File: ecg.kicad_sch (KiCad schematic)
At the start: 28 parts, among them SW1 SW_Push, SW2 SW_Push, U1 ESP32-S3-PICO-1-N8R2, U2 AD620, U3 OPA358

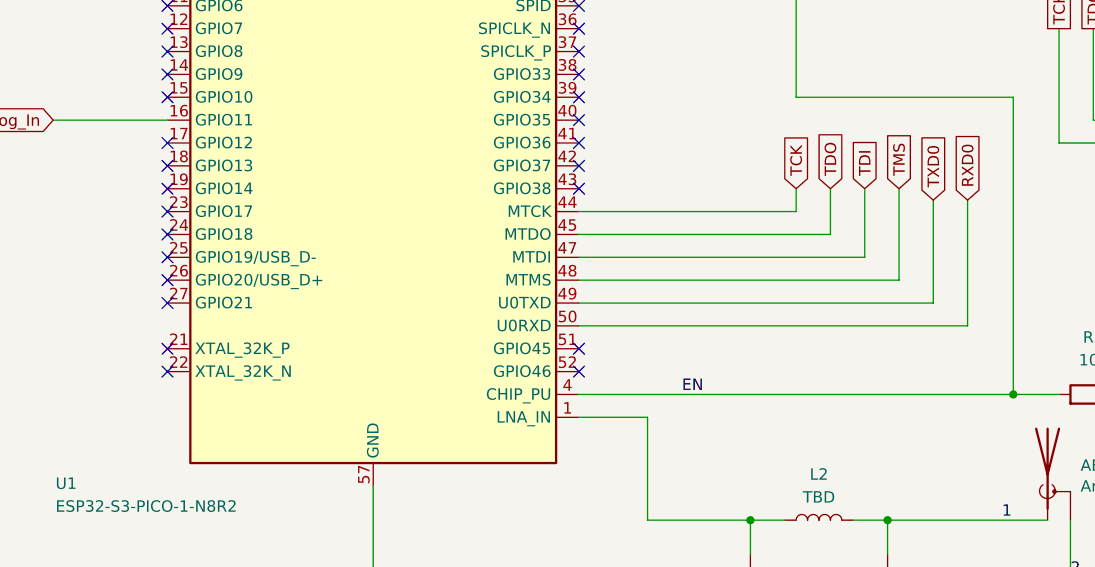
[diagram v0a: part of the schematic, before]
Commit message: Add 499ohm resistor for UART
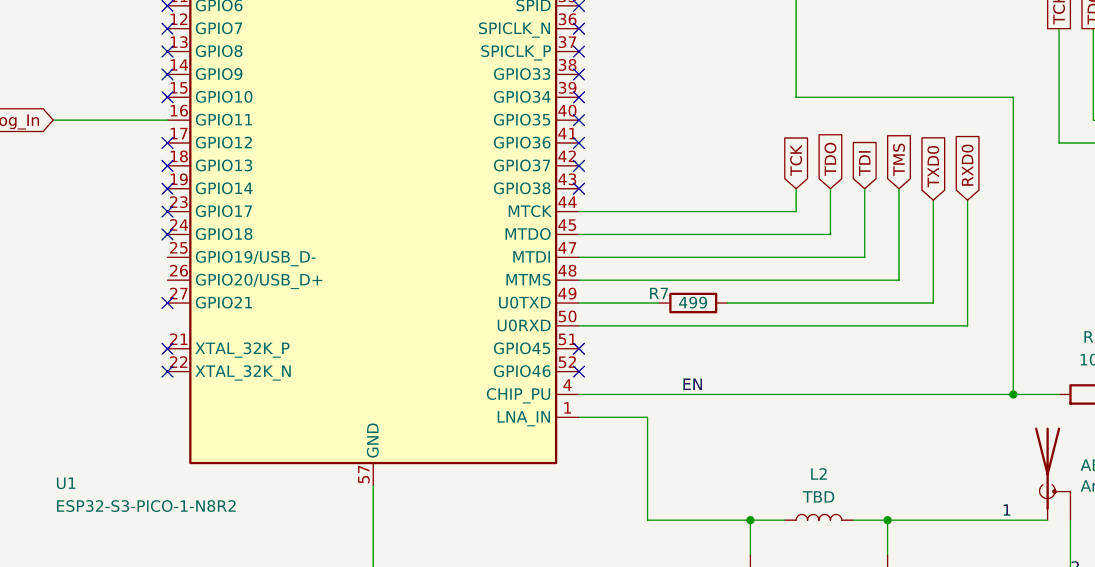
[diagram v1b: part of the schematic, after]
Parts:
- added R7: 499, symbol Device:R
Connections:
- net TDO: now also R7.2; no longer U1.49 (U0TXD)
- new net: R7.1, U1.49 (U0TXD)
- no-connect marks 38 -> 36
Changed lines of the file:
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@@
 	)
 	(no_connect
-		(at 86.36 154.94)
-	)
-	(no_connect
 		(at 86.36 139.7)
 	)
@@
 	)
 	(no_connect
-		(at 86.36 152.4)
-	)
-	(no_connect
 		(at 86.36 142.24)
 	)
@@
 	(wire
 		(pts
-			(xy 132.08 157.48) (xy 171.45 157.48)
-		)
-		(stroke
-			(width 0)
-			(type default)
-		)
-	)
-	(wire
-		(pts
 			(xy 368.3 134.62) (xy 368.3 162.56)
 		)
@@
 	(wire
 		(pts
+			(xy 148.59 157.48) (xy 171.45 157.48)
+		)
+		(stroke
+			(width 0)
+			(type default)
+		)
+	)
+	(wire
+		(pts
 			(xy 166.37 266.7) (xy 173.99 266.7)
 		)
@@
 	(wire
 		(pts
+			(xy 132.08 157.48) (xy 140.97 157.48)
+		)
+		(stroke
+			(width 0)
+			(type default)
+		)
+	)
+	(wire
+		(pts
 			(xy 166.37 196.85) (xy 151.13 196.85)
 		)
@@
 					(unit 1)
 				)
+			)
+		)
+	)
+	(symbol
+		(lib_id "Device:R")
+		(at 144.78 157.48 90)
+		(unit 1)
+		(exclude_from_sim no)
+		(in_bom yes)
+		(on_board yes)
+		(dnp no)
+		(property "Reference" "R7"
+			(at 140.97 156.464 90)
+			(effects
+				(font
+					(size 1.27 1.27)
+				)
+			)
+		)
+		(property "Value" "499"
+			(at 144.78 157.48 90)
+			(effects
+				(font
+					(size 1.27 1.27)
+				)
+			)
+		)
+		(property "Footprint" ""
+			(at 144.78 159.258 90)
+			(effects
+				(font
+					(size 1.27 1.27)
+				)
+				(hide yes)
+			)
+		)
+		(property "Datasheet" "~"
+			(at 144.78 157.48 0)
+			(effects
+				(font
+					(size 1.27 1.27)
+				)
+				(hide yes)
+			)
+		)
+		(property "Description" "Resistor"
+			(at 144.78 157.48 0)
+			(effects
+				(font
+					(size 1.27 1.27)
+				)
+				(hide yes)
+			)
+		)
+		(pin "2"
+		)
+		(pin "1"
+		)
+		(instances
+			(project "ecg"
+				(path "/78da8bdf-e40e-495b-ba6c-b18ee9000176"
+					(reference "R7")
+					(unit 1)
+				)

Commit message: A lot of changes!!!
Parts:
- removed AE2: Antenna_Shield, Connector_Coaxial:U.FL_Hirose_U.FL-R-SMT-1_Vertical, symbol Device:Antenna_Shield
- removed C7: 0.8 pF, Capacitor_SMD:C_0402_1005Metric, symbol Device:C
- removed L1: 3.9 nH, Inductor_SMD:L_0402_1005Metric, symbol Device:L
- added USB1: ~, symbol usb:USB_Blackbox
- AE1: footprint Connector_Coaxial:U.FL_Hirose_U.FL-R-SMT-1_Vertical -> RF_Antenna:Texas_SWRA117D_2.4GHz_Left
- C11, C12: value TBD -> 1.8 pF
- L2: value TBD -> 2.4 nH; footprint (none) -> Inductor_SMD:L_0201_0603Metric
- R7: footprint (none) -> Resistor_SMD:R_0201_0603Metric
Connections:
- net Analog_Out is gone; now on net Analog_In: C5.2, U3.1, U3.4 (-)
- net RXD0: no longer AE1.2 (Shield), BT1.2 (-), C1.1, C11.2, C12.2, C2.1, C3.1, C4.1, JTAG1. (4), SW1.1, SW2.1, U1.44 (MTCK), U1.47 (MTDI), U1.57 (GND), U2.4 (Vs-), U3.2 (V-)
- net TDO: no longer R7.2, UART1. (GND)
- net TMS: no longer AE1.1 (A), BT2.1 (+), C1.2, C11.1, C2.2, L2.2, R1.1, U1.2 (VDD3P3), U1.20 (VDD3P3_RTC), U1.3 (VDD3P3), U1.46 (VDD3P3_CPU), U1.55 (VDDA), U1.56 (VDDA), U2.7 (Vs+), U3.5 (ENABLE), U3.6 (V+), UART1. (GND)
- net USB_D-: now reaches U1.25 (GPIO19/USB_D-)
- net USB_D-: now also USB1. (2)
- net USB_D+: now reaches U1.26 (GPIO20/USB_D+)
- net USB_D+: now also USB1. (2)
- new net: BT2.1 (+), C1.2, C2.2, R1.1, U1.2 (VDD3P3), U1.20 (VDD3P3_RTC), U1.3 (VDD3P3), U1.46 (VDD3P3_CPU), U1.55 (VDDA), U1.56 (VDDA), U2.7 (Vs+), U3.5 (ENABLE), U3.6 (V+), UART1. (GND)
- new net 1: AE1.1 (A), C11.1, L2.2
- new net 2: AE1.2 (Shield), BT1.2 (-), C1.1, C11.2, C12.2, C2.1, C3.1, C4.1, SW1.1, SW2.1, U1.57 (GND), U2.4 (Vs-), U3.2 (V-), UART1. (GND)
- new net TCK: JTAG1. (4), U1.44 (MTCK)
- new net TDI: JTAG1. (4), U1.47 (MTDI)
- new net TXD0: R7.2, UART1. (GND)

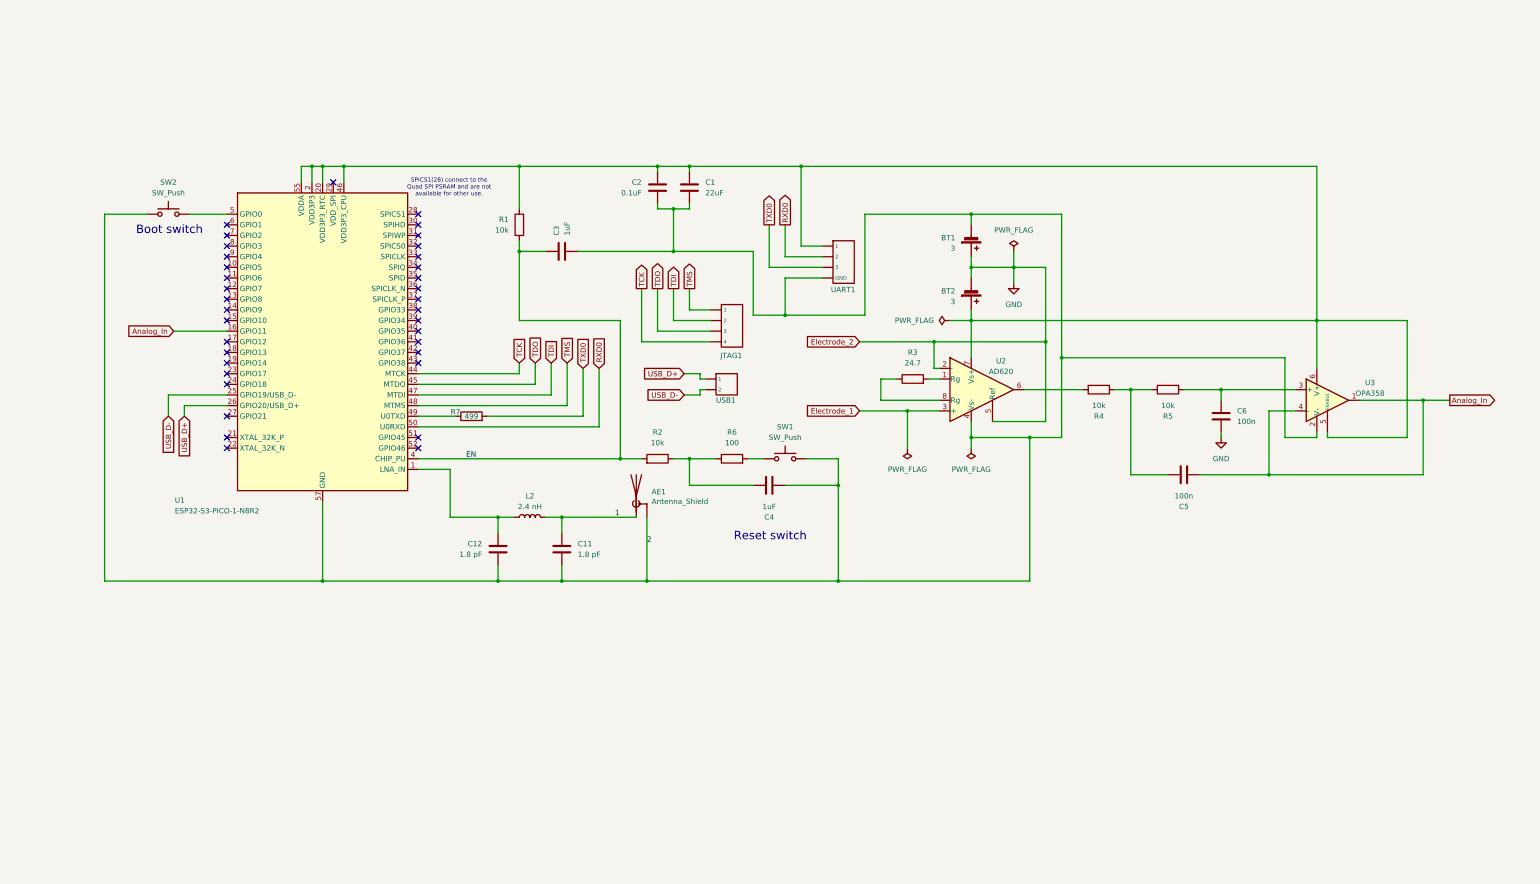
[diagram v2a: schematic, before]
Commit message: Added LDO
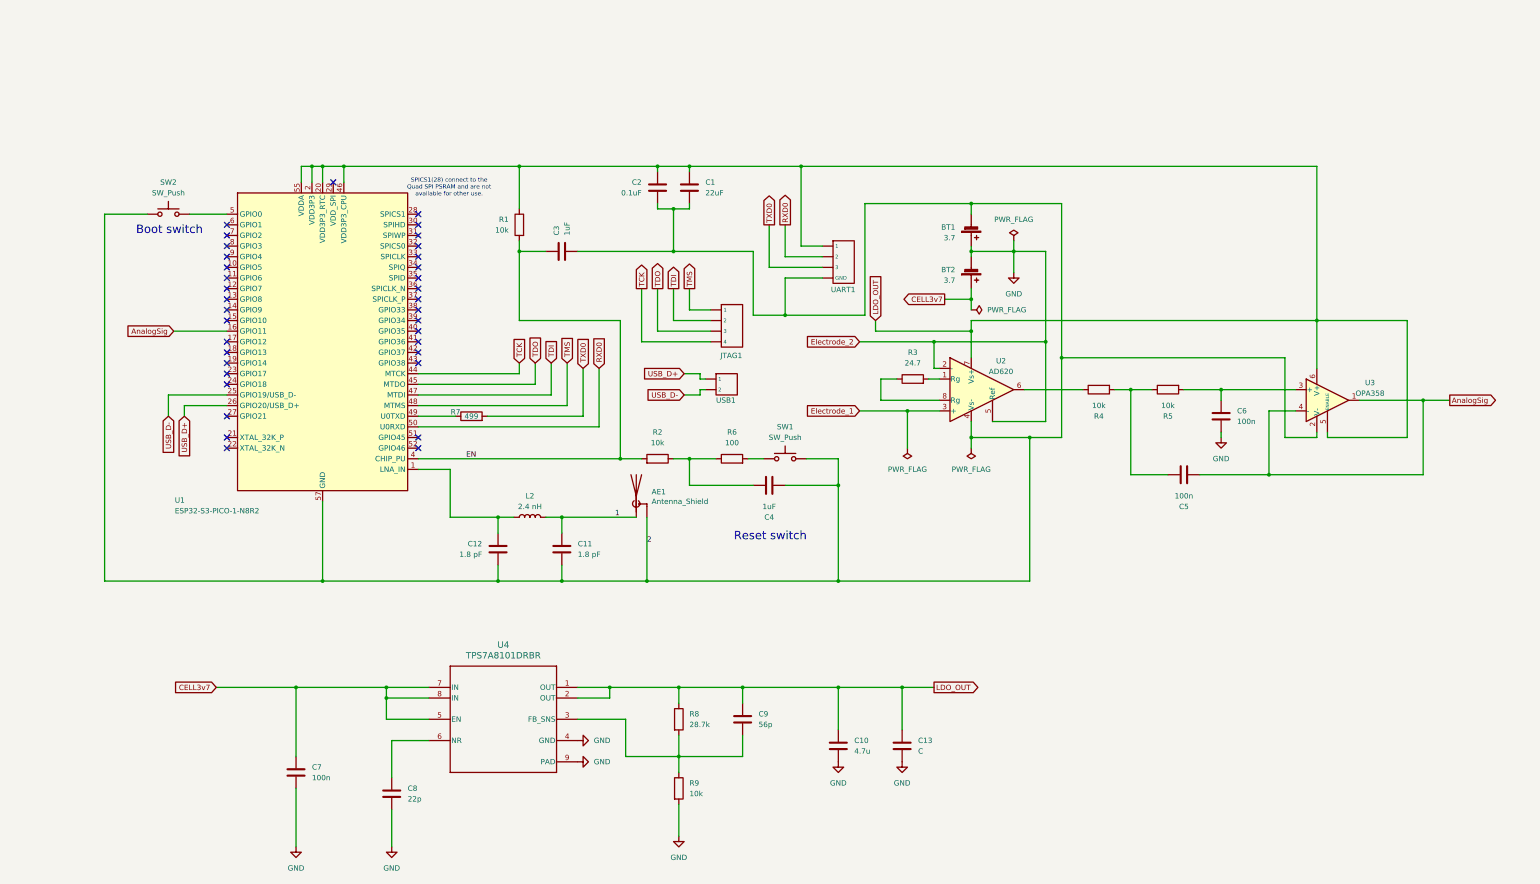
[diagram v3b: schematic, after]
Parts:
- added C10: 4.7u, symbol Device:C
- added C13: C, symbol Device:C
- added C7: 100n, symbol Device:C
- added C8: 22p, symbol Device:C
- added C9: 56p, symbol Device:C
- added R8: 28.7k, symbol Device:R
- added R9: 10k, symbol Device:R
- added U4: TPS7A8101DRBR, DRB0008A, symbol TPS7A8101DRBR:TPS7A8101DRBR
- BT1, BT2: value 3 -> 3.7
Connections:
- net GND: now also C10.2, C13.2, C7.2, C8.2, R9.2, U4.4 (GND), U4.9 (PAD)
- net LDO_OUT: now reaches C1.2, C2.2, R1.1, U1.2 (VDD3P3), U1.20 (VDD3P3_RTC), U1.3 (VDD3P3), U1.46 (VDD3P3_CPU), U1.55 (VDDA), U1.56 (VDDA), U2.7 (Vs+), U3.5 (ENABLE), U3.6 (V+), UART1. (GND)
- net LDO_OUT: now also C10.1, C13.1, C9.1, R8.1, U4.1 (OUT), U4.2 (OUT); no longer BT2.1 (+)
- net Analog_In renamed AnalogSig
- new net: C9.2, R8.2, R9.1, U4.3 (FB_SNS)
- new net: C8.1, U4.6 (NR)
- new net CELL3v7: BT2.1 (+), C7.1, U4.5 (EN), U4.7 (IN), U4.8 (IN)
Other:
- moved on the sheet: BT1, BT2

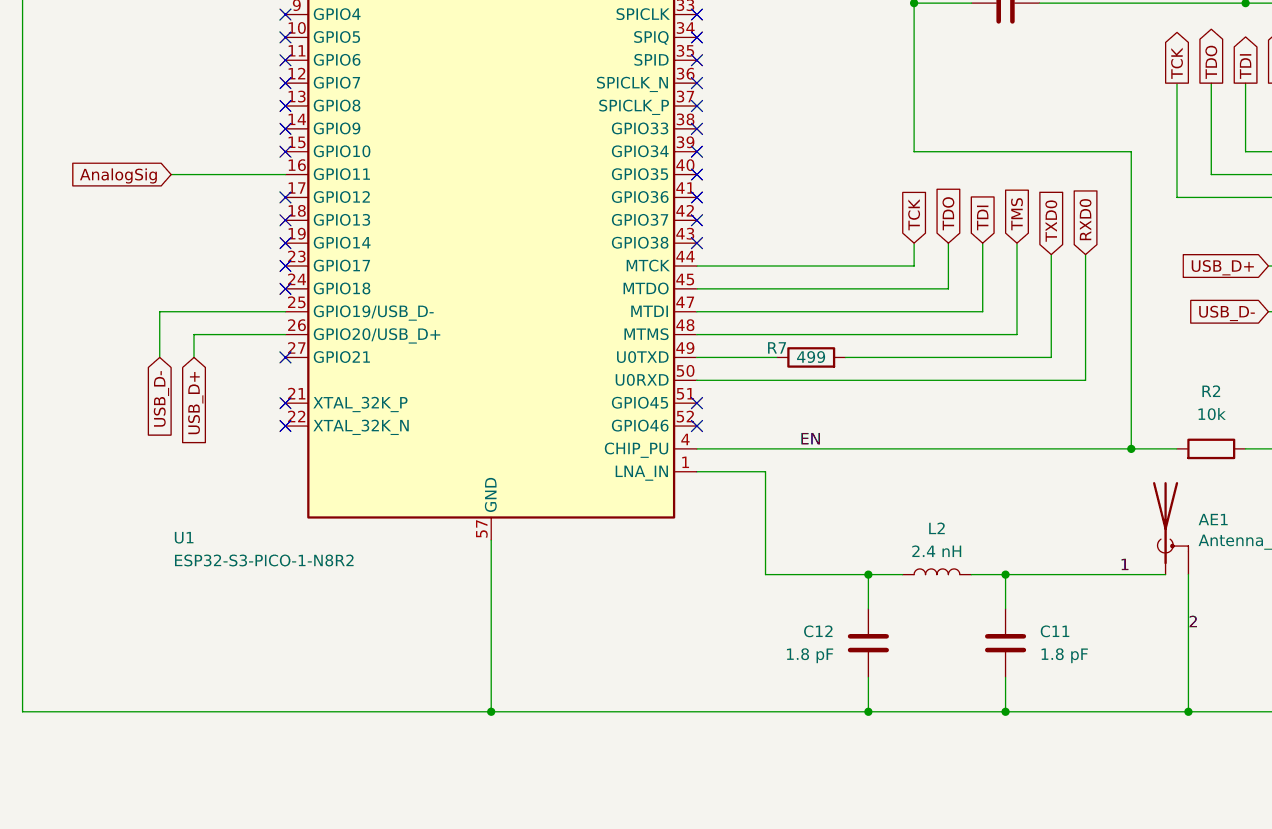
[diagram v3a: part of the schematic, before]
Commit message: Added Footprint for pin sockets and misc. changes
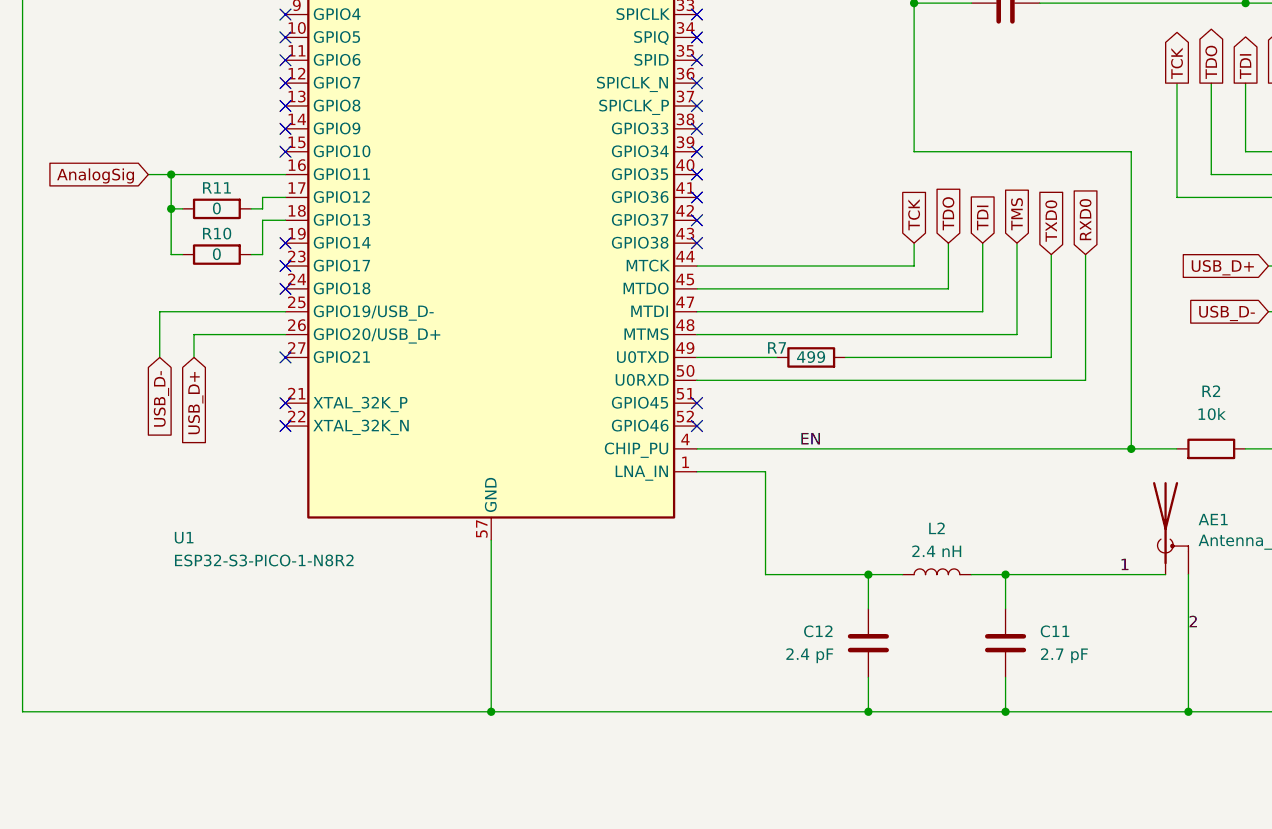
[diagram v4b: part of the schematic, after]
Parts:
- added R10, R11: 0, symbol Device:R
- C10, C13, C7, C8, C9: footprint (none) -> Capacitor_SMD:C_0201_0603Metric
- C11: value 1.8 pF -> 2.7 pF
- C12: value 1.8 pF -> 2.4 pF
- R8, R9: footprint (none) -> Resistor_SMD:R_0201_0603Metric
- U4: footprint DRB0008A -> (none)
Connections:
- net AnalogSig: now also R10.1, R11.1
- net at U1.17 (GPIO12): now also R11.2
- net at U1.18 (GPIO13): now also R10.2
- no-connect marks 36 -> 34
